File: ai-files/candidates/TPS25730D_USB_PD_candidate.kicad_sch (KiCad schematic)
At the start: 17 parts, among them J4 I2C service, U11 TPS25730DREFR, U19 TPS7B8450QWDRBRQ1

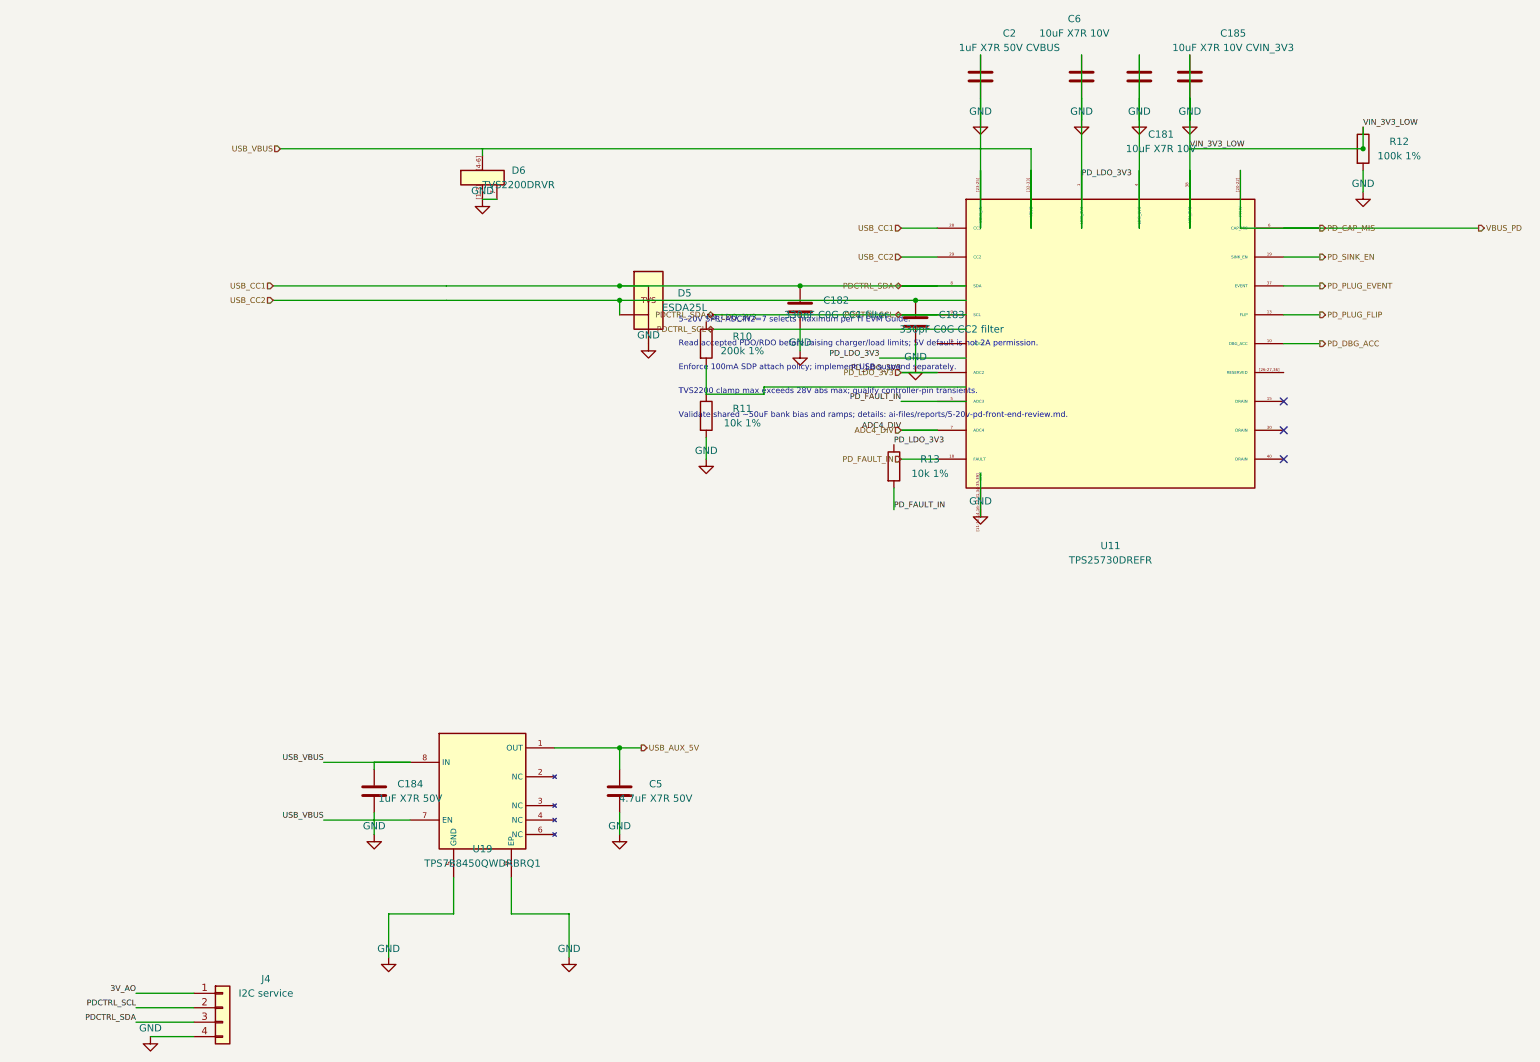
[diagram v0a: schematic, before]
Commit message: Redraw TPS25730D and BQ25792 candidates readable; record handoffs and 5-20 V PD scope decision
Co-Authored-By: Claude Sonnet 5.5 <noreply@anthropic.com>
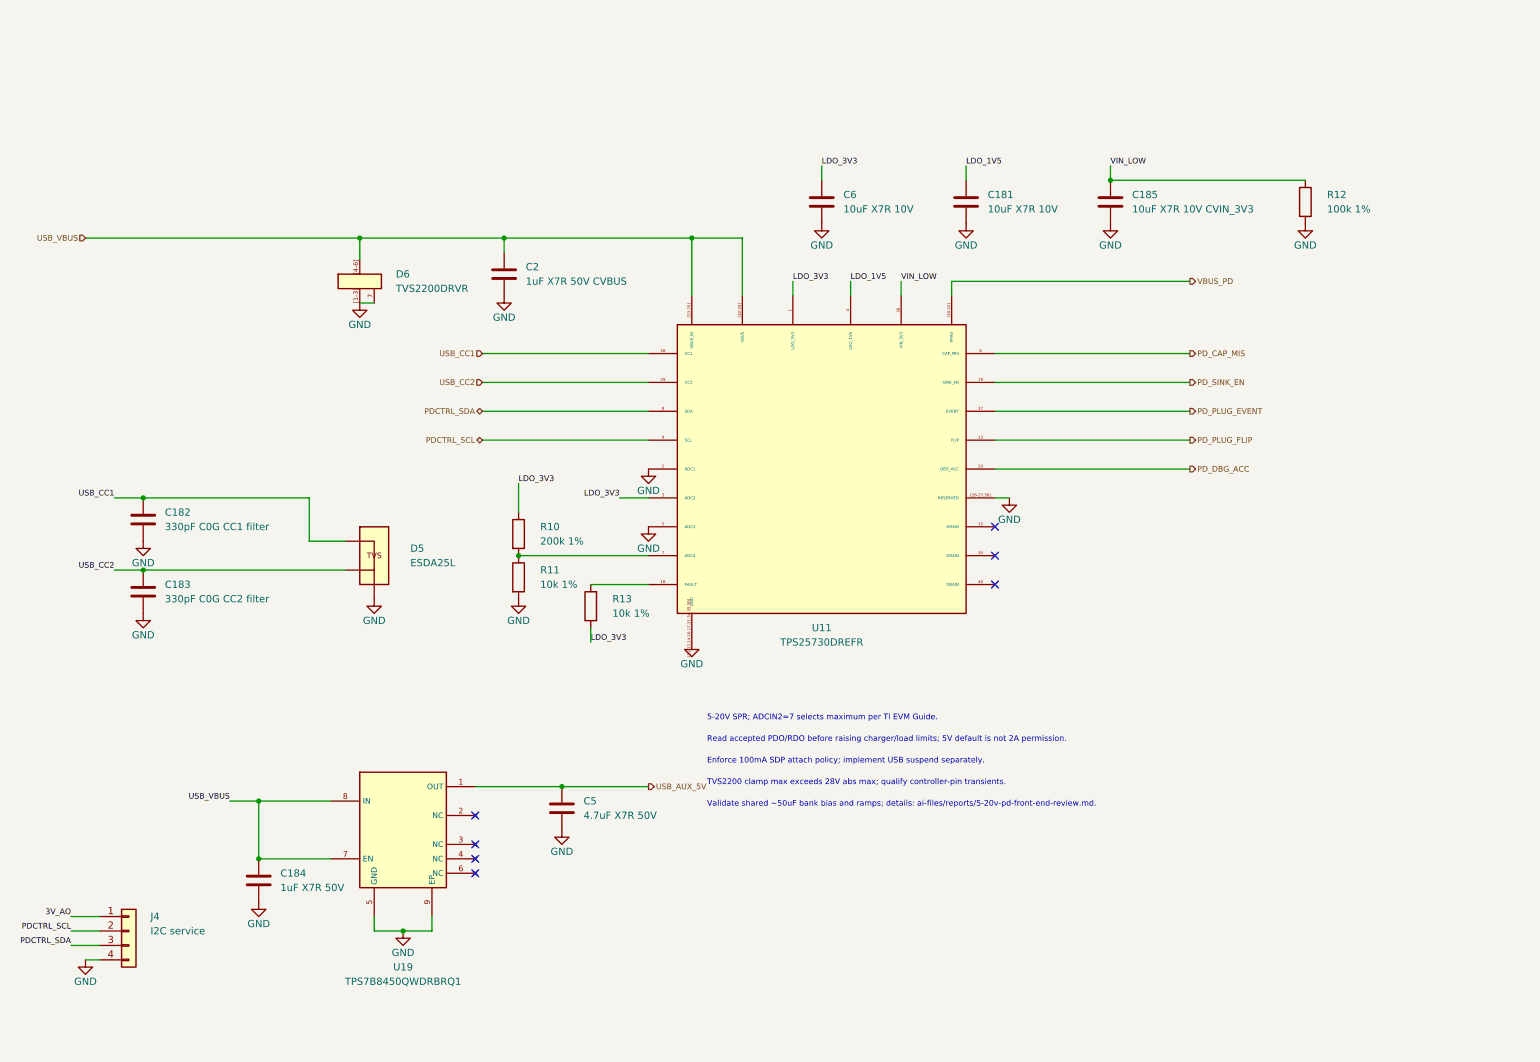
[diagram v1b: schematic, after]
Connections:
- net ADC4_DIV is gone; now on an unnamed net: U11.7 (ADC4)
- net GND: now also U11.2 (ADC1), U11.5 (ADC3), U11.[26-27,36] (RESERVED); no longer C181.1, C184.1, C185.1, C2.1, C6.1, D6.[4-6] (IN), R10.1, R12.1, R13.1, U11.1 (LDO_3V3), U11.3 (ADC2), U11.38 (VIN_3V3), U11.4 (LDO_1V5), U11.[23-25] (VBUS_IN), U11.[32-33] (VBUS), U19.7 (EN), U19.8 (IN)
- net PDCTRL_SCL: no longer C182.1, D5.1 (CC1/K1), J4.3 (Pin_3), U11.28 (CC1), U11.8 (SDA)
- net PD_CAP_MIS: no longer U11.[20-22] (PPHV)
- net PD_FAULT_IN: no longer names the net of R13.2, U11.18 (FAULT)
- new net LDO_1V5: C181.1, U11.4 (LDO_1V5)
- new net LDO_3V3: C6.1, R10.1, R13.1, U11.1 (LDO_3V3), U11.3 (ADC2)
- new net PDCTRL_SDA: J4.3 (Pin_3), U11.8 (SDA)
- new net USB_CC1: C182.1, D5.1 (CC1/K1), U11.28 (CC1)
- new net USB_VBUS: C184.1, C2.1, D6.[4-6] (IN), U11.[23-25] (VBUS_IN), U11.[32-33] (VBUS), U19.7 (EN), U19.8 (IN)
- new net VBUS_PD: U11.[20-22] (PPHV)
- new net VIN_LOW: C185.1, R12.1, U11.38 (VIN_3V3)
- no-connect marks 3 -> 7
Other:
- note added: "5-20V SPR; ADCIN2=7 selects maximum per TI EVM Guide."
- note removed: "5–20V SPR; ADCIN2=7 selects maximum per TI EVM Guide."
- moved on the sheet: U11, U19

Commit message: Apply Opus-reviewed must-fix items to PD and charger candidates
Co-Authored-By: Claude Sonnet 5.5 <noreply@anthropic.com>
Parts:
- added D7: 1N5819HW, DesktopSpeaker:PD_D_SOD123, symbol PD_DIODE:PD_DIODE
- added R14, R15, R18: 10k 1%, DesktopSpeaker:PD_R_0603, symbol PD_R:PD_R
- added R16, R17: 100k 1%, DesktopSpeaker:PD_R_0603, symbol PD_R:PD_R
- C2: value 1uF X7R 50V CVBUS -> 4.7uF X7R 50V; LCSC (none) -> C170099; LCSC Part (none) -> C170099; MPN (none) -> CL32B475KBUYNNE; Manufacturer (none) -> Samsung Electro-Mechanics
- C6: value 10uF X7R 10V -> 22uF X7R 10V; LCSC C32635 -> C907991; LCSC Part C32635 -> C907991; MPN CL21B106KPQNNNE -> GRM21BZ71A226ME15L; Manufacturer Samsung Electro-Mechanics -> Murata
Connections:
- net 3V_AO is gone; now on net LDO_3V3: J4.1 (Pin_1)
- net GND: now also U11.[26-27] (RESERVED), D7.2 (A), R18.2; no longer U11.[26-27,36] (RESERVED)
- net LDO_3V3: now also R14.1, R15.1, R16.2, R17.1
- net PDCTRL_SCL: now also R15.2
- net PDCTRL_SDA: now also R14.2
- net PD_PLUG_EVENT: now also R16.1
- net PD_SINK_EN: now also R17.2
- net USB_VBUS: now also D7.1 (K)
- net PD_CAP_MIS: no longer names the net of U11.6 (CAP_MIS)
- net PD_DBG_ACC: no longer names the net of U11.10 (DBG_ACC)
- net PD_PLUG_FLIP: no longer names the net of U11.13 (FLIP)
- new net: R18.1, U11.36 (RESERVED)
- no-connect marks 7 -> 10
